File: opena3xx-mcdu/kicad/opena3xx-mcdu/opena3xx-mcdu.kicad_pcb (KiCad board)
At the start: 2 copper layers, 145.3 x 224.3 mm, 145 parts, among them J1 Conn_02x01, J2 Conn_02x01, J3 Conn_02x01, J4 Conn_02x01, J5 Conn_02x01, J6 Conn_02x01, J7 Conn_02x01, J8 Conn_02x01, J9 Conn_02x01, SW1 TLL-6A, SW10 TLL-6A, SW100 SW_MEC_5E, SW11 TLL-6A, SW12 TLL-6A, SW13 TLL-6A, SW14 TLL-6A, SW15 TLL-6A, SW16 TLL-6A, SW17 TLL-6A, SW18 TLL-6A, SW19 TLL-6A, SW2 TLL-6A, SW20 TLL-6A, SW21 TLL-6A, SW22 TLL-6A, SW23 TLL-6A, SW24 TLL-6A, SW25 TLL-6A, SW26 TLL-6A, SW27 TLL-6A, SW28 TLL-6A, SW29 TLL-6A, SW3 TLL-6A, SW30 TLL-6A, SW31 TLL-6A, SW32 TLL-6A, SW33 TLL-6A, SW34 TLL-6A, SW35 TLL-6A, SW36 TLL-6A, SW37 TLL-6A, SW38 TLL-6A, SW39 TLL-6A, SW4 TLL-6A, SW40 TLL-6A, SW41 TLL-6A, SW42 TLL-6A, SW43 TLL-6A, SW44 TLL-6A, SW45 TLL-6A, SW46 TLL-6A, SW47 TLL-6A, SW48 TLL-6A, SW49 TLL-6A, SW5 TLL-6A, SW50 TLL-6A, SW51 TLL-6A, SW52 TLL-6A, SW53 TLL-6A, SW54 TLL-6A, SW55 TLL-6A, SW56 TLL-6A, SW57 TLL-6A, SW58 TLL-6A, SW59 TLL-6A, SW6 TLL-6A, SW60 TLL-6A, SW61 TLL-6A, SW62 TLL-6A, SW63 TLL-6A, SW64 TLL-6A, SW65 TLL-6A, SW66 TLL-6A, SW67 TLL-6A, SW68 TLL-6A, SW69 TLL-6A, SW7 TLL-6A, SW70 TLL-6A, SW8 TLL-6A, SW9 TLL-6A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

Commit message: Continuation of MCDU PCB v0.1
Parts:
- J1, J2: moved to B.Cu
- moved R35 192.8 mm to (164.7, 181.4)
- moved R36 192.1 mm to (164.6, 194.4)
- moved R23 191.2 mm to (189.2, 230.6)
- moved R33 186.4 mm to (220.1, 241.5)
- moved D11 180.5 mm to (139.6, 209.8), turned to 90 degrees
- moved R26 176.5 mm to (205.1, 185.4)
- moved R21 170.3 mm to (189.1, 206.5)
- moved R34 169.1 mm to (265.6, 241.4)
- moved R22 168.2 mm to (189.1, 218.4)
- moved R32 166.7 mm to (250.1, 227.5)
- moved D9 164.6 mm to (139.8, 192.0), turned to 90 degrees
- moved R28 164.5 mm to (220.1, 199.5)
- moved R31 158.3 mm to (205.1, 227.5)
- moved R24 143.3 mm to (189.0, 242.3)
- moved R29 135.9 mm to (265.5, 199.3)
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
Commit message: Updated PCB MCDU v0.1
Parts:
- removed the J1 at (274.7, 163.8)
- removed the J2 at (274.7, 156.2)
- removed J8, J9: Conn_02x01, TerminalBlock:TerminalBlock_bornier-2_P5.08mm
- added REF**: OSHW-Logo2_14.6x12mm_SilkScreen, Symbol:OSHW-Logo2_14.6x12mm_SilkScreen, F.Cu at (204.3, 54.7)
- D1, D2, D3, D4, R1, R10, R11, R12, R2, R3, R4, R5, R6, R7, R8, R9: moved to B.Cu
- moved R41 193.3 mm to (144.8, 191.9), turned to 90 degrees
- moved R43 191.1 mm to (144.7, 209.9), turned to 90 degrees
- moved D4 189.9 mm to (155.3, 32.0), turned to 180 degrees
- moved R2 183.5 mm to (157.4, 40.5), turned to 270 degrees
- moved R3 177.2 mm to (165.8, 40.5), turned to 270 degrees
- moved R12 163.9 mm to (146.4, 47.1), turned to 180 degrees
- moved R1 163.0 mm to (153.5, 40.5), turned to 270 degrees
- moved R4 157.6 mm to (161.6, 40.5), turned to 270 degrees
- moved J3 147.2 mm to (274.0, 228.5), turned to 270 degrees
- moved R8 135.7 mm to (201.2, 82.7), turned to 90 degrees
- moved J4 135.2 mm to (273.9, 218.1), turned to 270 degrees
- moved R39 129.2 mm to (190.8, 38.4)
- moved R40 121.6 mm to (205.6, 38.4)
- moved R42 113.2 mm to (265.7, 193.6), turned to 180 degrees
- moved R5 104.5 mm to (226.5, 82.8), turned to 90 degrees
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- renumbered J3 to J1, J4 to J2, J6 to J3, J7 to J4
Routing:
- net GND: track 0.00 -> 1749.9 mm, vias 0 -> 3
- net +12V: track 0.00 -> 756.7 mm, vias 0 -> 4
- net +5V: track 0.00 -> 527.9 mm, vias 0 -> 9
- net /BUS3-8: track 0.00 -> 187.2 mm
- net /BUS2-1: track 0.00 -> 183.7 mm, vias 0 -> 2
- net /BUS4-12: track 0.00 -> 176.8 mm, vias 0 -> 3
- net /BUS2-2: track 0.00 -> 173.0 mm, vias 0 -> 2
- net /BUS4-10: track 0.00 -> 169.9 mm, vias 0 -> 3
- net /BUS3-9: track 0.00 -> 166.0 mm, vias 0 -> 4
- net /BUS0-11: track 0.00 -> 164.5 mm, vias 0 -> 2
- net /BUS4-5: track 0.00 -> 163.5 mm, vias 0 -> 2
- net BUSES_RESET: track 0.00 -> 162.5 mm, vias 0 -> 5
- net /BUS2-3: track 0.00 -> 159.6 mm, vias 0 -> 2
- net /BUS4-3: track 0.00 -> 159.2 mm, vias 0 -> 2
- net /BUS3-3: track 0.00 -> 158.0 mm, vias 0 -> 3
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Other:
- outline, holes or cut-outs redrawn
- board text added: "FM1"
- board text added: "FM2"
- board text added: "IND"
- board text added: "LSK1"
- board text added: "LSK2"
- board text added: "LSK3"
- board text added: "LSK4"
- board text added: "LSK5"
- board text added: "LSK6"
- board text added: "OPENA3XX IS OPEN-SOURCE HARDWARE & SOFTWARE"
- board text added: "RDY"
- board text added: "https://www.github.com/opena3xx"

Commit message: Finalised Layour for MCDU PCB v 0.1
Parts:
- removed REF**: OSHW-Logo2_14.6x12mm_SilkScreen, Symbol:OSHW-Logo2_14.6x12mm_SilkScreen
- added G***: LOGO, openaa3xx:logo-bsilkscreen, F.Cu at (216.5, 125.7)
- added J6: Conn_02x01, TerminalBlock:TerminalBlock_bornier-2_P5.08mm, B.Cu at (274.0, 136.3)
- added J7: Conn_02x01, TerminalBlock:TerminalBlock_bornier-2_P5.08mm, B.Cu at (274.0, 125.6)
- added R44: 220R, Resistor_SMD:R_1210_3225Metric_Pad1.30x2.65mm_HandSolder, F.Cu at (261.2, 132.7)
- added SW71: TLL-6A, openaa3xx:TACTILE_LED_TH, F.Cu at (262.1, 136.0)
- added SW72: TLL-6A, openaa3xx:TACTILE_LED_TH, F.Cu at (262.2, 149.2)
- moved G*** 33.0 mm to (205.7, 56.0)
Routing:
- net GND: track 1749.9 -> 0.00 mm, vias 3 -> 0
- net +12V: track 756.7 -> 0.00 mm, vias 4 -> 0
- net +5V: track 527.9 -> 0.00 mm, vias 9 -> 0
- net /BUS3-8: track 187.2 -> 0.00 mm
- net /BUS2-1: track 183.7 -> 0.00 mm, vias 2 -> 0
- net /BUS4-12: track 176.8 -> 0.00 mm, vias 3 -> 0
- net /BUS2-2: track 173.0 -> 0.00 mm, vias 2 -> 0
- net /BUS4-10: track 169.9 -> 0.00 mm, vias 3 -> 0
- net /BUS3-9: track 166.0 -> 0.00 mm, vias 4 -> 0
- net /BUS0-11: track 164.5 -> 0.00 mm, vias 2 -> 0
- net /BUS4-5: track 163.5 -> 0.00 mm, vias 2 -> 0
- net BUSES_RESET: track 162.5 -> 0.00 mm, vias 5 -> 0
- net /BUS2-3: track 159.6 -> 0.00 mm, vias 2 -> 0
- net /BUS4-3: track 159.2 -> 0.00 mm, vias 2 -> 0
- net /BUS3-3: track 158.0 -> 0.00 mm, vias 3 -> 0
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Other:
- outline, holes or cut-outs redrawn

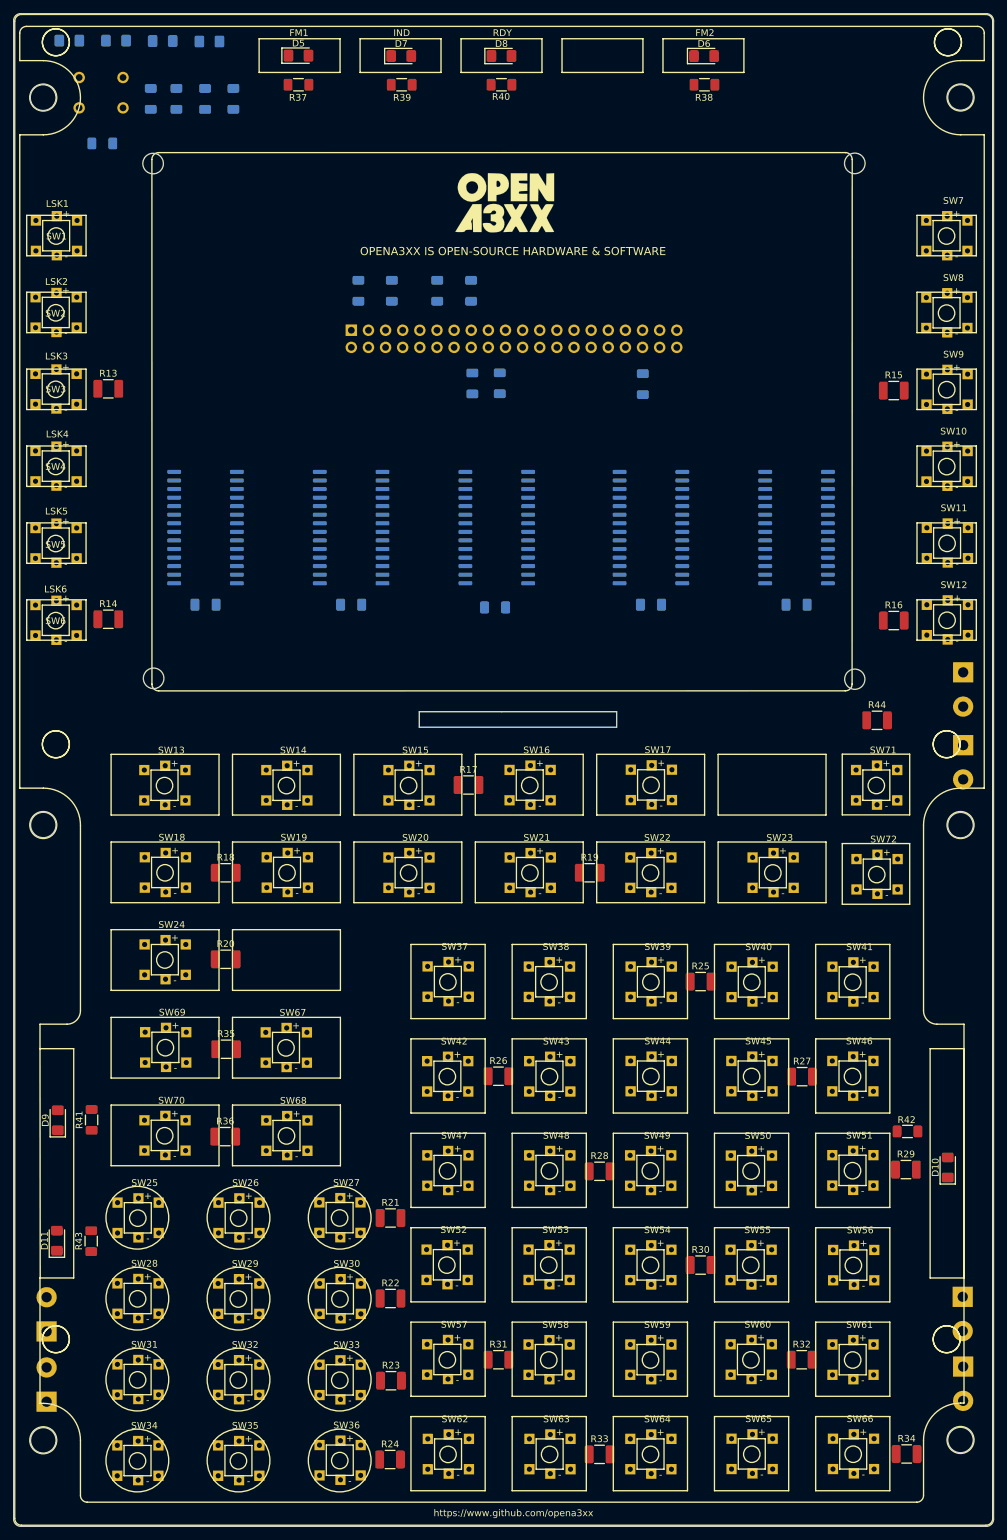
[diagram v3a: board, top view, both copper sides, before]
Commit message: Fixing PCB dimensions for the MCDU
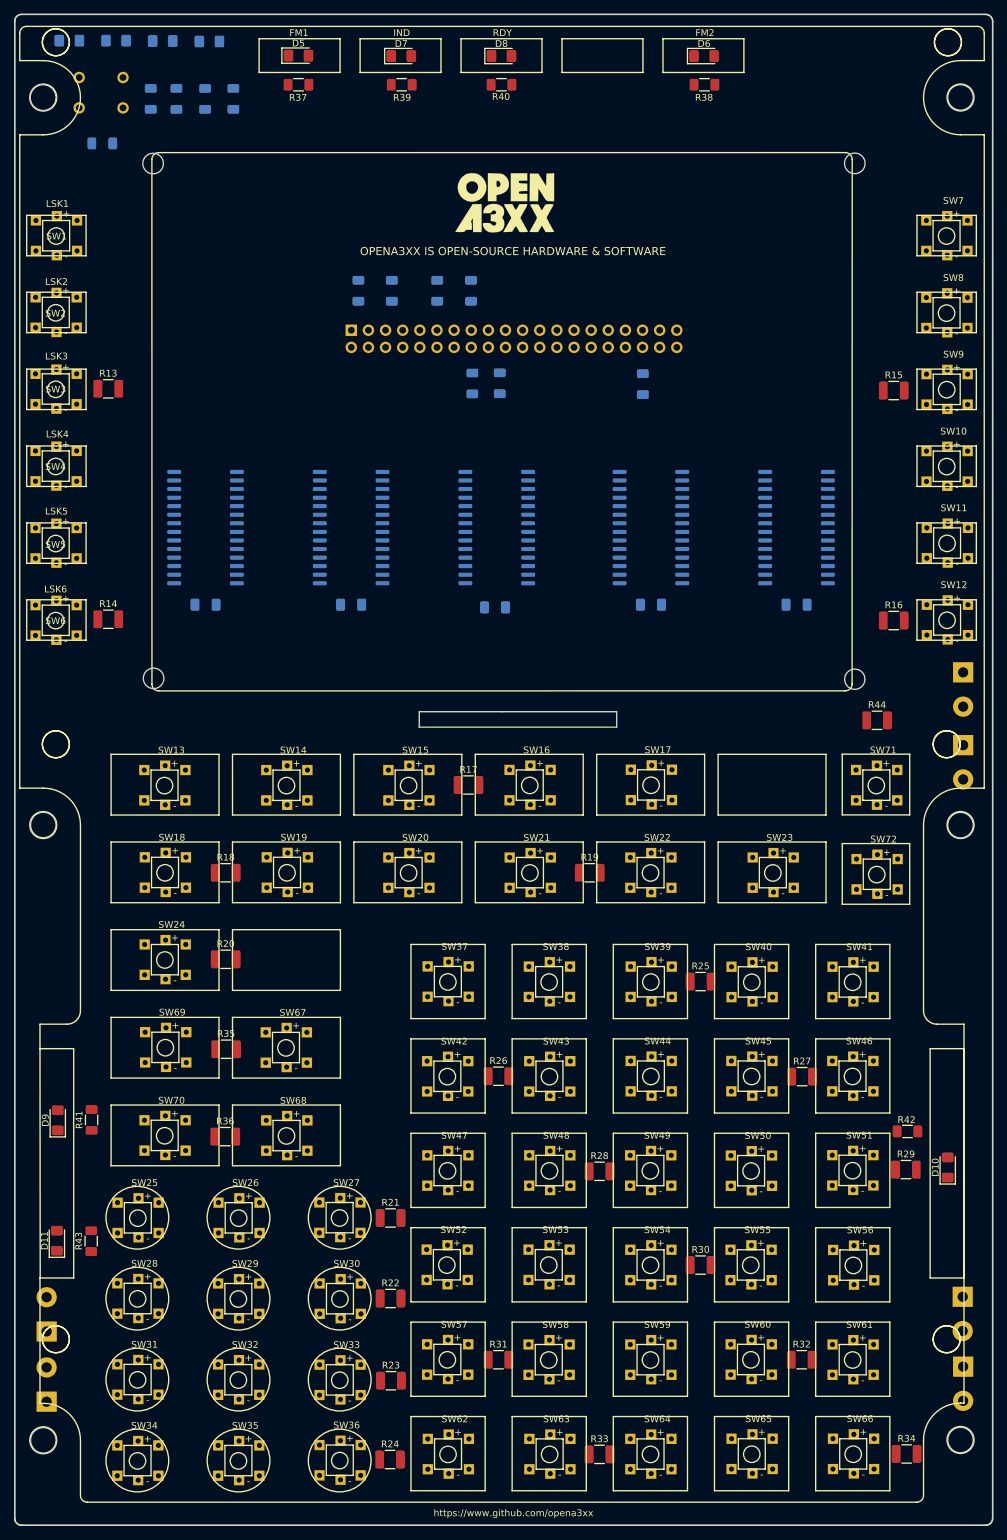
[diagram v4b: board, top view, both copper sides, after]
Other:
- board size 145.3 x 224.3 mm -> 145 x 224 mm

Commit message: PCB MCDU changes
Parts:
- removed G***: LOGO, openaa3xx:logo-bsilkscreen
- removed G***: LOGO, openaa3xx:logo
- moved J3 0.27 mm to (273.9, 228.8)
- moved J1 0.19 mm to (138.1, 233.9)
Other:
- board size 145 x 224 mm -> 267.2 x 225 mm
- board text added: "RSK1"
- board text added: "RSK2"
- board text added: "RSK3"
- board text added: "RSK4"

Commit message: Minor changes MCDU PCB
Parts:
- moved R10 2.18 mm to (182.2, 69.0)
- moved R11 2.18 mm to (187.1, 69.0)
- moved R6 2.18 mm to (193.8, 69.0)
- moved R7 2.18 mm to (198.9, 69.0)
- moved J5 2.18 mm to (181.1, 74.9)
- moved R8 2.18 mm to (199.0, 82.8)
- moved R5 2.18 mm to (224.3, 82.9)
- moved R9 2.18 mm to (203.1, 82.7)
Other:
- board size 267.2 x 225 mm -> 148 x 225 mm
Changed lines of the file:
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@@
   (general
     (thickness 1.6)
-    (drawings 628)
+    (drawings 623)
     (tracks 0)
     (zones 0)
@@
     (aux_axis_origin 0 0)
     (grid_origin 278.511 27.8892)
-    (visible_elements 7FF8F11F)
+    (visible_elements 7FF9F11F)
     (pcbplotparams
       (layerselection 0x010fc_ffffffff)
@@
   )
   (module Resistor_SMD:R_1206_3216Metric_Pad1.30x1.75mm_HandSolder (layer B.Cu)
-    (at 189.294 68.9737 90)
+    (at 187.1096 69.0245 90)
     (descr "Resistor SMD 1206 (3216 Metric), square (rectangular) end terminal, IPC_7351 nominal with elongated pad for handsoldering. (Body size source: IPC-SM-782 page 72, https://www.pcb-3d.com/wordpress/wp-content/uploads/ipc-sm-782a_amendment_1_and_2.pdf), generated with kicad-footprint-generator")
     (tags "resistor handsolder")
@@
   )
   (module Resistor_SMD:R_1206_3216Metric_Pad1.30x1.75mm_HandSolder (layer B.Cu)
-    (at 184.34 68.9737 90)
+    (at 182.1556 69.0245 90)
     (descr "Resistor SMD 1206 (3216 Metric), square (rectangular) end terminal, IPC_7351 nominal with elongated pad for handsoldering. (Body size source: IPC-SM-782 page 72, https://www.pcb-3d.com/wordpress/wp-content/uploads/ipc-sm-782a_amendment_1_and_2.pdf), generated with kicad-footprint-generator")
     (tags "resistor handsolder")
@@
   )
   (module Resistor_SMD:R_1206_3216Metric_Pad1.30x1.75mm_HandSolder (layer B.Cu)
-    (at 205.296 82.6897 90)
+    (at 203.1116 82.7405 90)
     (descr "Resistor SMD 1206 (3216 Metric), square (rectangular) end terminal, IPC_7351 nominal with elongated pad for handsoldering. (Body size source: IPC-SM-782 page 72, https://www.pcb-3d.com/wordpress/wp-content/uploads/ipc-sm-782a_amendment_1_and_2.pdf), generated with kicad-footprint-generator")
     (tags "resistor handsolder")
@@
   )
   (module Resistor_SMD:R_1206_3216Metric_Pad1.30x1.75mm_HandSolder (layer B.Cu)
-    (at 201.232 82.7157 90)
+    (at 199.0476 82.7665 90)
     (descr "Resistor SMD 1206 (3216 Metric), square (rectangular) end terminal, IPC_7351 nominal with elongated pad for handsoldering. (Body size source: IPC-SM-782 page 72, https://www.pcb-3d.com/wordpress/wp-content/uploads/ipc-sm-782a_amendment_1_and_2.pdf), generated with kicad-footprint-generator")
     (tags "resistor handsolder")
@@
   )
   (module Resistor_SMD:R_1206_3216Metric_Pad1.30x1.75mm_HandSolder (layer B.Cu)
-    (at 201.041 68.9737 270)
+    (at 198.8566 69.0245 270)
     (descr "Resistor SMD 1206 (3216 Metric), square (rectangular) end terminal, IPC_7351 nominal with elongated pad for handsoldering. (Body size source: IPC-SM-782 page 72, https://www.pcb-3d.com/wordpress/wp-content/uploads/ipc-sm-782a_amendment_1_and_2.pdf), generated with kicad-footprint-generator")
     (tags "resistor handsolder")
@@
   )
   (module Resistor_SMD:R_1206_3216Metric_Pad1.30x1.75mm_HandSolder (layer B.Cu)
-    (at 196.024 68.9737 270)
+    (at 193.8396 69.0245 270)
     (descr "Resistor SMD 1206 (3216 Metric), square (rectangular) end terminal, IPC_7351 nominal with elongated pad for handsoldering. (Body size source: IPC-SM-782 page 72, https://www.pcb-3d.com/wordpress/wp-content/uploads/ipc-sm-782a_amendment_1_and_2.pdf), generated with kicad-footprint-generator")
     (tags "resistor handsolder")
@@
   )
   (module Resistor_SMD:R_1206_3216Metric_Pad1.30x1.75mm_HandSolder (layer B.Cu)
-    (at 226.504 82.8167 90)
+    (at 224.3196 82.8675 90)
     (descr "Resistor SMD 1206 (3216 Metric), square (rectangular) end terminal, IPC_7351 nominal with elongated pad for handsoldering. (Body size source: IPC-SM-782 page 72, https://www.pcb-3d.com/wordpress/wp-content/uploads/ipc-sm-782a_amendment_1_and_2.pdf), generated with kicad-footprint-generator")
     (tags "resistor handsolder")
@@
   )
   (module Connector_PinHeader_2.54mm:PinHeader_2x20_P2.54mm_Vertical (layer B.Cu)
-    (at 183.286 74.8284 270)
+    (at 181.1016 74.8792 270)
     (descr "Through hole straight pin header, 2x20, 2.54mm pitch, double rows")
     (tags "Through hole pin header THT 2x20 2.54mm double row")
@@
     )
   )
-  (dimension 142.999999 (width 0.12) (layer B.SilkS)
-    (gr_text "143.000 mm" (at 205.62802 47.192855 0.002563084642) (layer B.SilkS)
-      (effects (font (size 1 1) (thickness 0.15)))
-    )
-    (feature1 (pts (xy 277.12796 45.84777) (xy 277.127989 46.506078)))
-    (feature2 (pts (xy 134.127961 45.854167) (xy 134.12799 46.512475)))
-    (crossbar (pts (xy 134.127964 45.926054) (xy 277.127963 45.919657)))
-    (arrow1a (pts (xy 277.127963 45.919657) (xy 276.001485 46.506128)))
-    (arrow1b (pts (xy 277.127963 45.919657) (xy 276.001433 45.333287)))
-    (arrow2a (pts (xy 134.127964 45.926054) (xy 135.254494 46.512424)))
-    (arrow2b (pts (xy 134.127964 45.926054) (xy 135.254442 45.339583)))
-  )
   (gr_line (start 276.12796 29.775074) (end 135.127961 29.775074) (layer F.SilkS) (width 0.2))
   (gr_arc (start 135.127961 30.775074) (end 135.127961 29.775074) (angle -90) (layer F.SilkS) (width 0.2))
@@
     (effects (font (size 1 1) (thickness 0.15)))
   )
-  (gr_circle (center 293.1414 149.097789) (end 294.6654 149.123189) (layer Edge.Cuts) (width 0.05))
-  (gr_circle (center 293.2176 225.424789) (end 293.2176 223.900789) (layer Edge.Cuts) (width 0.05))
-  (gr_circle (center 397.1798 225.551789) (end 398.6784 225.602589) (layer Edge.Cuts) (width 0.05))
-  (gr_circle (center 397.1798 149.072389) (end 398.7038 149.097789) (layer Edge.Cuts) (width 0.05))
   (gr_line (start 217.934718 137.397239) (end 217.934718 146.997238) (layer F.SilkS) (width 0.2))
   (gr_line (start 235.934718 159.997238) (end 219.334718 159.997238) (layer F.SilkS) (width 0.2))
@@
     (effects (font (size 1 1) (thickness 0.15)))
   )
-  (gr_arc (start 175.006 50.4317) (end 175.006 49.4157) (angle -90) (layer B.SilkS) (width 0.12))
-  (gr_arc (start 239.3315 50.4317) (end 240.3475 50.4317) (angle -90) (layer B.SilkS) (width 0.12))
-  (gr_arc (start 175.006 78.1812) (end 173.99 78.1812) (angle -90) (layer B.SilkS) (width 0.12))
-  (gr_arc (start 239.3315 78.1812) (end 239.3315 79.1972) (angle -90) (layer B.SilkS) (width 0.12))
-  (gr_line (start 240.3475 50.4317) (end 240.3475 78.1812) (layer B.SilkS) (width 0.12))
-  (gr_line (start 175.006 49.4157) (end 239.3315 49.4157) (layer B.SilkS) (width 0.12))
-  (gr_line (start 173.99 78.1812) (end 173.99 50.4317) (layer B.SilkS) (width 0.12))
-  (gr_line (start 239.3315 79.1972) (end 175.006 79.1972) (layer B.SilkS) (width 0.12))
+  (gr_arc (start 172.8216 50.4825) (end 172.8216 49.4665) (angle -90) (layer B.SilkS) (width 0.12))
+  (gr_arc (start 237.1471 50.4825) (end 238.1631 50.4825) (angle -90) (layer B.SilkS) (width 0.12))
+  (gr_arc (start 172.8216 78.232) (end 171.8056 78.232) (angle -90) (layer B.SilkS) (width 0.12))
+  (gr_arc (start 237.1471 78.232) (end 237.1471 79.248) (angle -90) (layer B.SilkS) (width 0.12))
+  (gr_line (start 238.1631 50.4825) (end 238.1631 78.232) (layer B.SilkS) (width 0.12))
+  (gr_line (start 172.8216 49.4665) (end 237.1471 49.4665) (layer B.SilkS) (width 0.12))
+  (gr_line (start 171.8056 78.232) (end 171.8056 50.4825) (layer B.SilkS) (width 0.12))
+  (gr_line (start 237.1471 79.248) (end 172.8216 79.248) (layer B.SilkS) (width 0.12))
   (gr_line (start 137.16 215.3412) (end 137.127961 181.346305) (layer F.SilkS) (width 0.2))
   (gr_line (start 193.3575 132.8674) (end 205.613 132.8674) (layer Edge.Cuts) (width 0.05))
